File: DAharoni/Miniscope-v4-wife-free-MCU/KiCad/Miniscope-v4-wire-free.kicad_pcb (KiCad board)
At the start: 6 copper layers, 17 x 12.5 mm, 42 parts, among them J1 0475710001, J10 Conn_01x20, J2 Conn_01x01, J3 Conn_01x05, J4 Conn_01x01, J5 Conn_01x01, J6 Conn_01x01, J8 Conn_01x01, J9 Conn_01x01, U1 TPS62402-Q1, U2 MAX13030EETE+, U3 ATSAME70N21A-CN, Y1 ABM8G-12.000MHZ-4Y-T3

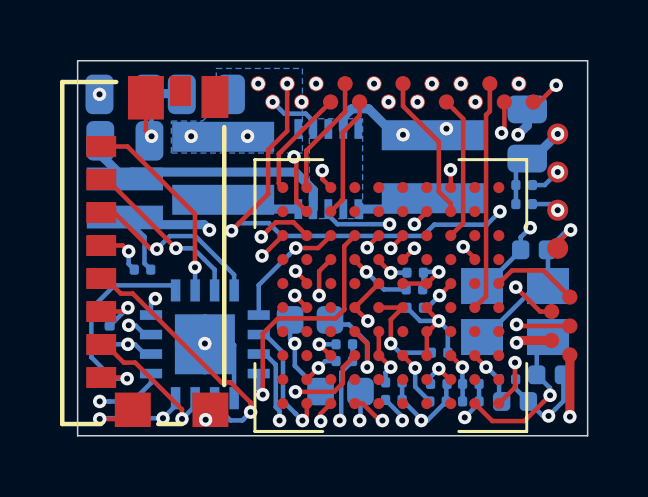
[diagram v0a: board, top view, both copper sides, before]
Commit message: Finish wire-free MCU PCB and flexPC for first fab run (version 0.1)
The committed gerbers were submitted to JLCPCB and PCBway on 09/21/2019
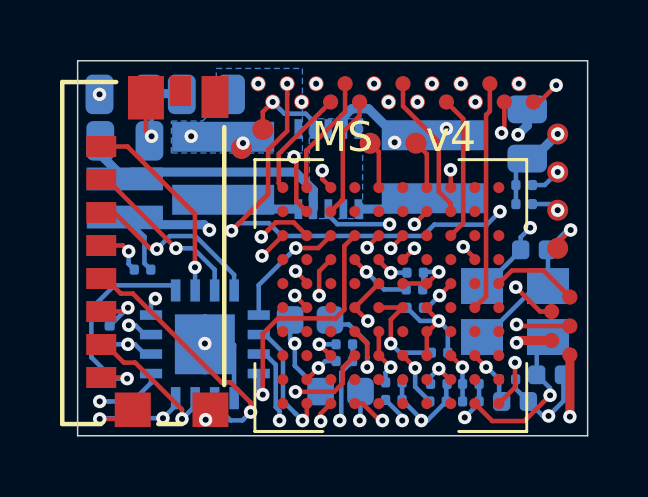
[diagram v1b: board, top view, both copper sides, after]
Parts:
- added J11: Conn_01x01, .Connector:Conn_1x1_700_Circular_Pad, F.Cu at (112.3, 88.2)
- added J12: Conn_01x01, .Connector:Conn_1x1_700_Circular_Pad, F.Cu at (106.5, 88.4)
- added J13: Conn_01x01, .Connector:Conn_1x1_700_Circular_Pad, F.Cu at (107.2, 87.8)
- added J7: Conn_01x01, .Connector:Conn_1x1_700_Circular_Pad, F.Cu at (110.8, 88.2)
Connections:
- U3 pad C1: /IR_REV -> Net-(U3-PadC1)
- U3 pad D2: /STATUS_LED -> Net-(U3-PadD2)
- U3 pad K4: Net-(U3-PadK4) -> /STATUS_LED
- U3 pad K6: Net-(U3-PadK6) -> /IR_REV
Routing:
- net /STATUS_LED: track 0.00 -> 1.63 mm
- net /IR_REV: track 0.00 -> 1.60 mm
- net GND: track 45.8 -> 46.9 mm
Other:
- board text added: "GND"
- board text added: "MS v4"
- board text added: "WF-v0.1"
